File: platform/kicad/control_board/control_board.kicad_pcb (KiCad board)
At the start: 2 copper layers, 81.5 x 131.5 mm, 71 parts, among them J1 DHT22, J10 ADC1,7, J11 Qwiic JST, J12 Data 1, J13 Data 2, J14 ROUTER 24V, J15 24V/5V OUT, J16 Data 3, J17 PoE 2, J18 Conn_01x03, J19 Conn_01x03, J2 DS18B20, J3 Conn_01x04, J4 24V IN, J5 Conn_01x05_Pin, J6 PoE 1, J7 PoE 3, J8 UART, J9 ADC1,6, K1 LCA717, K2 LCA717, K3 LCA717, K4 LCA717, U1 ESP32-DevKitC, U2 ACS722xLCTR-20AU, U3 AP63205WU-7, U4 AP63205WU-7

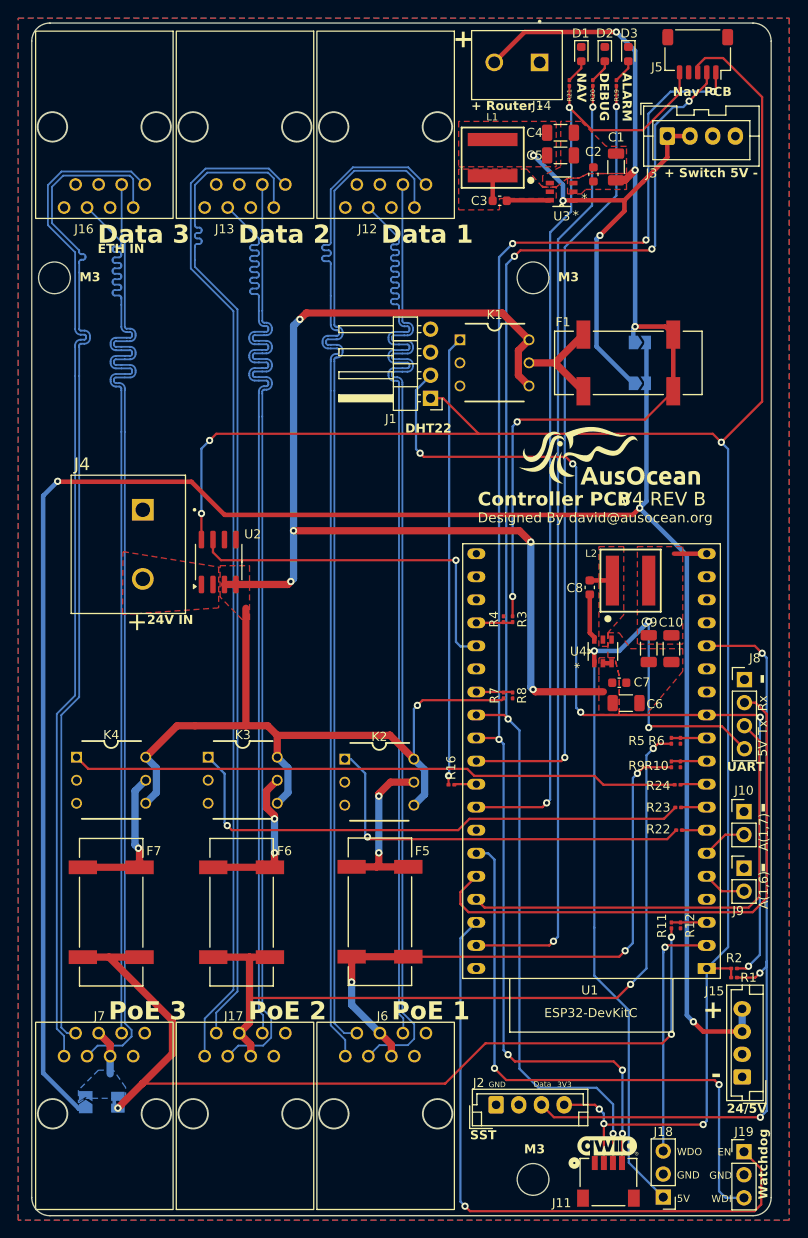
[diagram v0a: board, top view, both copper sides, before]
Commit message: Controller: Upsize resistors
This change alters the resistor footprints from 0201 to 0603 which allows the cheaper
PCBA method to be used, decreasing the cost of the board.
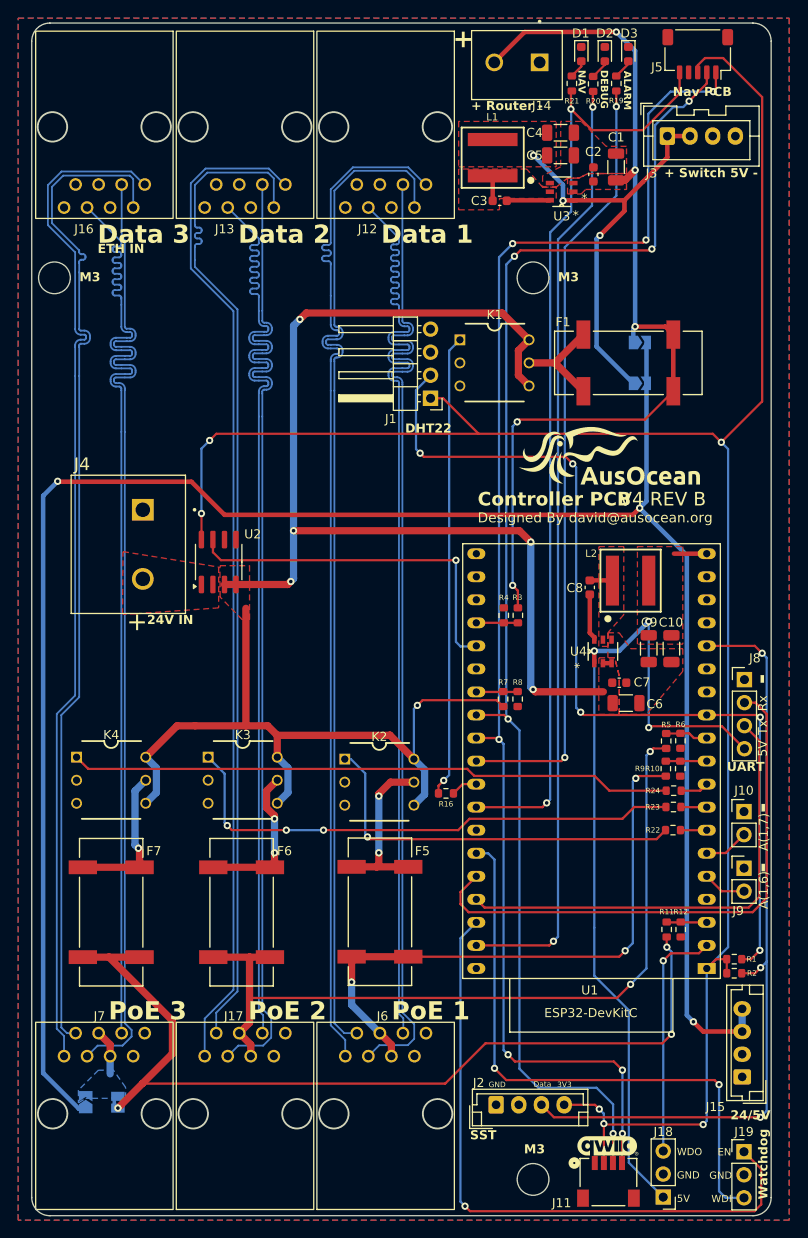
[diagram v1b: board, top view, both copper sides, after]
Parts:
- R1, R10, R11, R12, R16, R19, R2, R20, R21, R22, R23, R24, R3, R4, R5, R6, R7, R8, R9: footprint Resistor_SMD:R_0201_0603Metric -> Resistor_SMD:R_0603_1608Metric
- moved R16 1.12 mm to (131.3, 110.1)
- moved R1 1.03 mm to (163.1, 128.4)
- moved R24 0.78 mm to (156.4, 109.8)
- moved R9 0.78 mm to (155.6, 107.4)
- moved R3 0.72 mm to (139.3, 90.5)
- moved R11 0.69 mm to (155.7, 125.1)
- moved R8 0.68 mm to (139.2, 99.7)
- moved R22 0.67 mm to (156.4, 114.2)
- moved R5 0.57 mm to (155.6, 104.3)
- moved R23 0.53 mm to (156.4, 111.6)
- moved R2 0.48 mm to (163.1, 129.9)
- moved R10 0.48 mm to (157.2, 107.4)
- moved R12 0.45 mm to (157.2, 125.1)
- moved R4 0.43 mm to (137.7, 90.5)
- moved R7 0.40 mm to (137.6, 99.7)
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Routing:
- net Net-(K1-+CONTROL): track 49.6 -> 51.0 mm
- net DHT: track 103.8 -> 102.6 mm
- net P1_out: track 67.3 -> 66.1 mm
- net Net-(K2-+CONTROL): track 44.6 -> 43.4 mm
- net SST: track 87.1 -> 86.1 mm
- net Net-(K3-+CONTROL): track 59.0 -> 58.0 mm, vias 1 -> 3
- net EN: track 27.4 -> 26.5 mm
- net Navlight: track 105.4 -> 104.5 mm
- net _P2_out: track 3.91 -> 4.69 mm
- net P2_out: track 90.0 -> 89.3 mm
- net P3_out: track 100.5 -> 99.8 mm
- net NW_out: track 103.6 -> 102.9 mm
- net Net-(K4-+CONTROL): track 67.2 -> 66.5 mm
- net _P1_out: track 3.92 -> 4.52 mm
- net LED0: track 104.8 -> 104.2 mm
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
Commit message: Controller: Move fuse before relay and add test points (#21)
This change moves the fuse before the relay to prevent the relay from still being powered (and potentially short circuit)
after the fuse has blow. This change also adds LED indicators for the relay status, as well as adding test points for
the control signal of each relay.
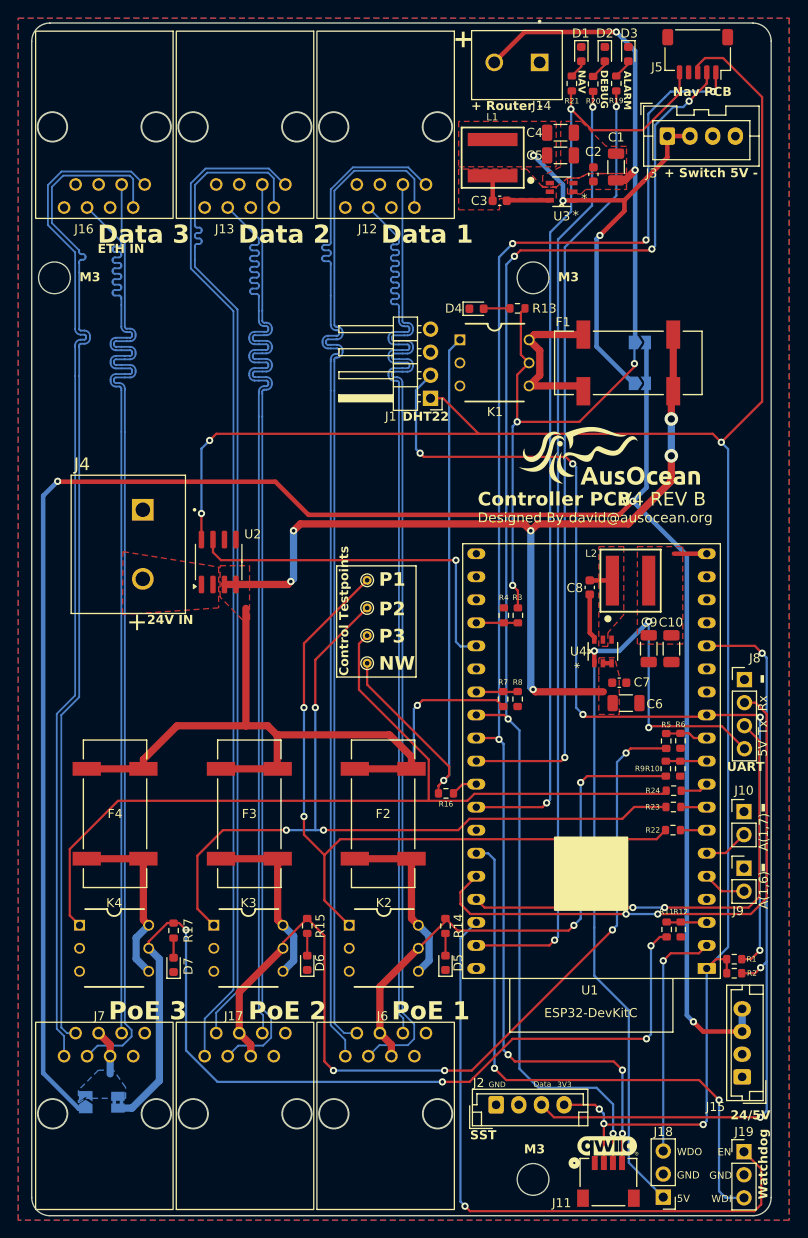
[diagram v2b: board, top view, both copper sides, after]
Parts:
- removed F5, F6, F7: 3588TR, AusOcean:3588TR_FUSE_HOLDER
- added D4: APHD1608LZGCK, LED_SMD:LED_0603_1608Metric, F.Cu at (134.7, 56.7)
- added D5: APHD1608LZGCK, LED_SMD:LED_0603_1608Metric, F.Cu at (131.3, 128.8)
- added D6: APHD1608LZGCK, LED_SMD:LED_0603_1608Metric, F.Cu at (116.1, 128.8)
- added D7: APHD1608LZGCK, LED_SMD:LED_0603_1608Metric, F.Cu at (101.3, 129.0)
- added F2: 3588TR, AusOcean:3588TR_FUSE_HOLDER, F.Cu at (124.4, 112.4)
- added F3: 3588TR, AusOcean:3588TR_FUSE_HOLDER, F.Cu at (109.7, 112.4)
- added F4: 3588TR, AusOcean:3588TR_FUSE_HOLDER, F.Cu at (94.9, 112.4)
- added R13: 12K 1/4 W, Resistor_SMD:R_0603_1608Metric, F.Cu at (139.2, 56.7)
- added R14: 12K 1/4 W, Resistor_SMD:R_0603_1608Metric, F.Cu at (131.3, 124.7)
- added R15: 12K 1/4 W, Resistor_SMD:R_0603_1608Metric, F.Cu at (116.1, 124.7)
- added R17: 12K 1/4 W, Resistor_SMD:R_0603_1608Metric, F.Cu at (101.3, 125.2)
- added TP1: TestPoint, TestPoint:TestPoint_THTPad_D1.0mm_Drill0.5mm, F.Cu at (122.7, 95.8)
- added TP2: TestPoint, TestPoint:TestPoint_THTPad_D1.0mm_Drill0.5mm, F.Cu at (122.7, 86.6)
- added TP3: TestPoint, TestPoint:TestPoint_THTPad_D1.0mm_Drill0.5mm, F.Cu at (122.7, 89.7)
- added TP4: TestPoint, TestPoint:TestPoint_THTPad_D1.0mm_Drill0.5mm, F.Cu at (122.7, 92.7)
- moved K3 18.5 mm to (109.6, 127.2)
- moved K4 18.5 mm to (94.8, 127.2)
- moved K2 18.3 mm to (124.5, 127.2)
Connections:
- F1 pad 1: NW_out -> 24VIN
- F1 pad 2: NW_out -> 24VIN
- F1 pad 3: Net-(K1-LOAD-) -> Net-(K1-LOAD1)
- F1 pad 4: Net-(K1-LOAD-) -> Net-(K1-LOAD1)
- K1 pad 4: 24VIN -> Net-(K1-LOAD1)
- K1 pad 5: Net-(K1-LOAD-) -> NW_out
- K1 pad 6: 24VIN -> Net-(K1-LOAD1)
- K2 pad 4: 24VIN -> Net-(K2-LOAD1)
- K2 pad 5: Net-(K2-LOAD-) -> P1_out
- K2 pad 6: 24VIN -> Net-(K2-LOAD1)
- K3 pad 4: 24VIN -> Net-(K3-LOAD1)
- K3 pad 5: Net-(K3-LOAD-) -> P2_out
- K3 pad 6: 24VIN -> Net-(K3-LOAD1)
- K4 pad 4: 24VIN -> Net-(K4-LOAD1)
- K4 pad 5: Net-(K4-LOAD-) -> P3_out
- K4 pad 6: 24VIN -> Net-(K4-LOAD1)
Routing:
- net Net-(K2-+CONTROL): track 43.4 -> 81.7 mm, vias 1 -> 2
- net Net-(K4-+CONTROL): track 66.5 -> 99.0 mm
- net Net-(K3-+CONTROL): track 58.0 -> 89.1 mm
- net Net-(K4-LOAD1): track 0.00 -> 20.3 mm
- net Net-(K2-LOAD1): track 0.00 -> 20.0 mm
- net Net-(K3-LOAD1): track 0.00 -> 19.9 mm
- net Net-(K2-LOAD-): track 18.8 -> 0.00 mm, vias 2 -> 0
- net Net-(K1-LOAD1): track 0.00 -> 18.5 mm
- net Net-(K1-+CONTROL): track 51.0 -> 67.9 mm
- net Net-(K3-LOAD-): track 16.9 -> 0.00 mm, vias 2 -> 0
- net 24VIN: track 203.5 -> 186.7 mm, vias 6 -> 7
- net Net-(K4-LOAD-): track 16.5 -> 0.00 mm, vias 1 -> 0
- net Net-(K1-LOAD-): track 11.7 -> 0.00 mm
- net P2_out: track 89.3 -> 98.7 mm, vias 2 -> 4
- net P3_out: track 99.8 -> 106.9 mm, vias 3 -> 4
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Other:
- board text added: "Control Testpoints"
- board text added: "P1"
- board text added: "P2"

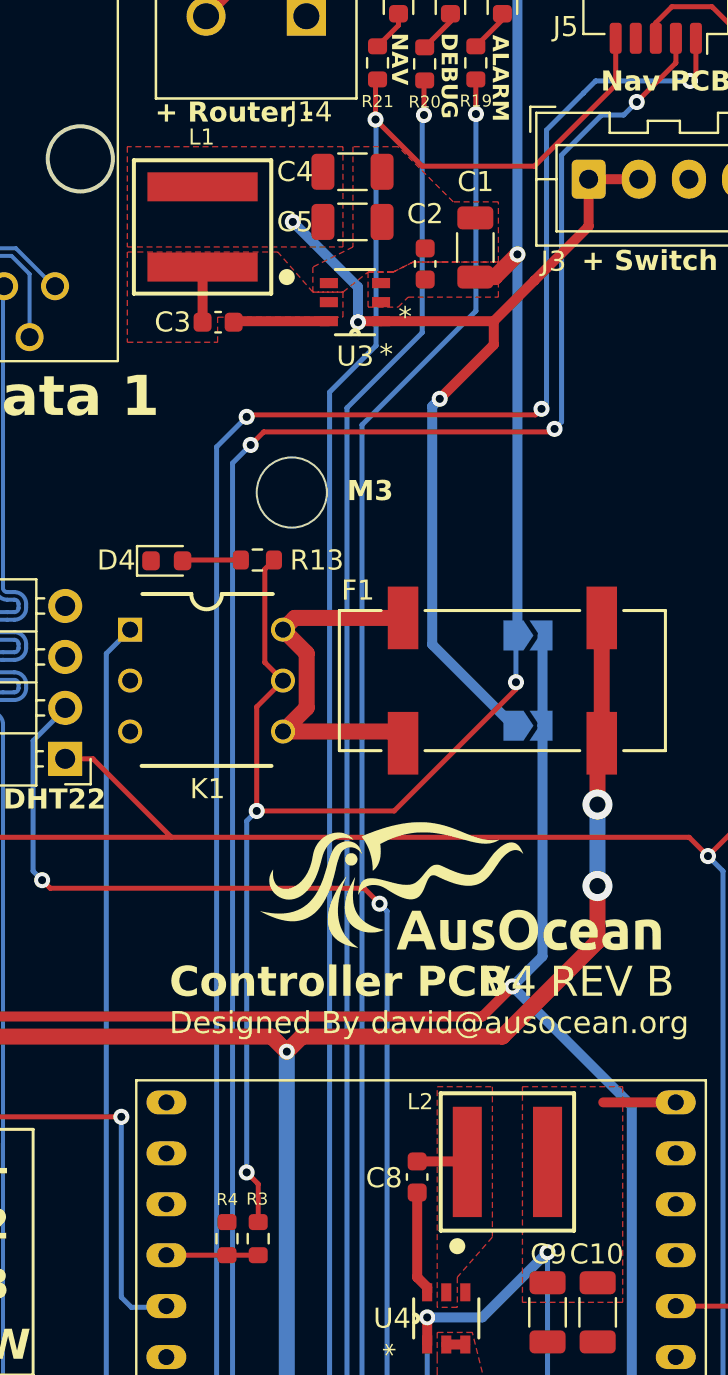
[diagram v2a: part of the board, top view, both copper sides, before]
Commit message: Controller: Finalise for production
This change updates the production files
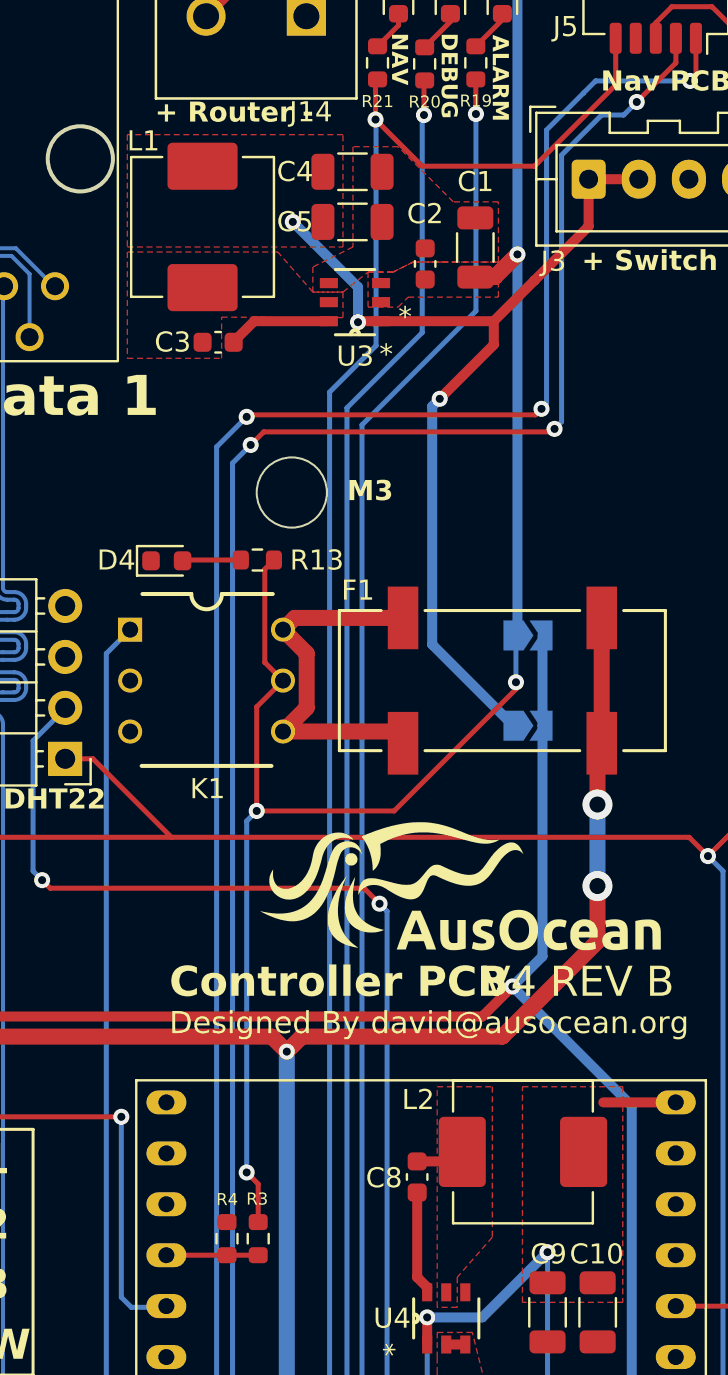
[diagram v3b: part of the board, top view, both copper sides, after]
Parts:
- L1, L2: footprint AusOcean:WE-XHMI_6060 -> Inductor_SMD:L_Changjiang_FXL0630
- moved C3 1.00 mm to (137.3, 45.8)
- moved L2 0.92 mm to (152.5, 86.2), turned to 0 degrees
- turned L1 to 90 degrees
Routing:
- net Net-(U3-SW): track 2.75 -> 0.00 mm
